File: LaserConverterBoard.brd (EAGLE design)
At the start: 100 x 80 mm, 49 parts, among them J10 24V, J11 FAN, J12 E-STOP, J3 04-JST-B4B-XH-A, J4 04-JST-B4B-XH-A, J5 04-JST-B4B-XH-A, J6 X, J7 Y, J8 Z-STOP, Q1 FDN5630, Q2 FDN5630, U10 REE-0505S, Y1 POLOLU_A4988, Y2 POLOLU_A4988, Y3 POLOLU_A4988

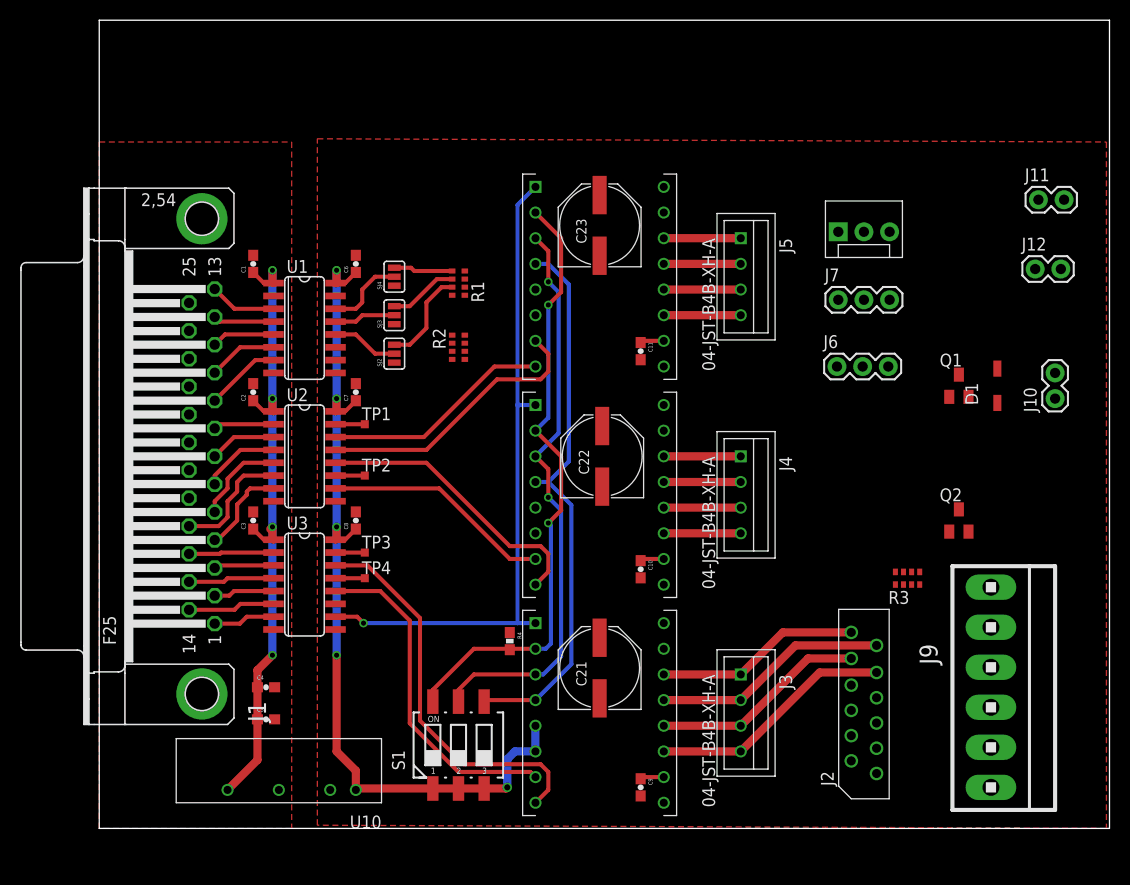
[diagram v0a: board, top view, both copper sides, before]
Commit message: Hand routing of board 1.3 complete. Still needs silk screening done.
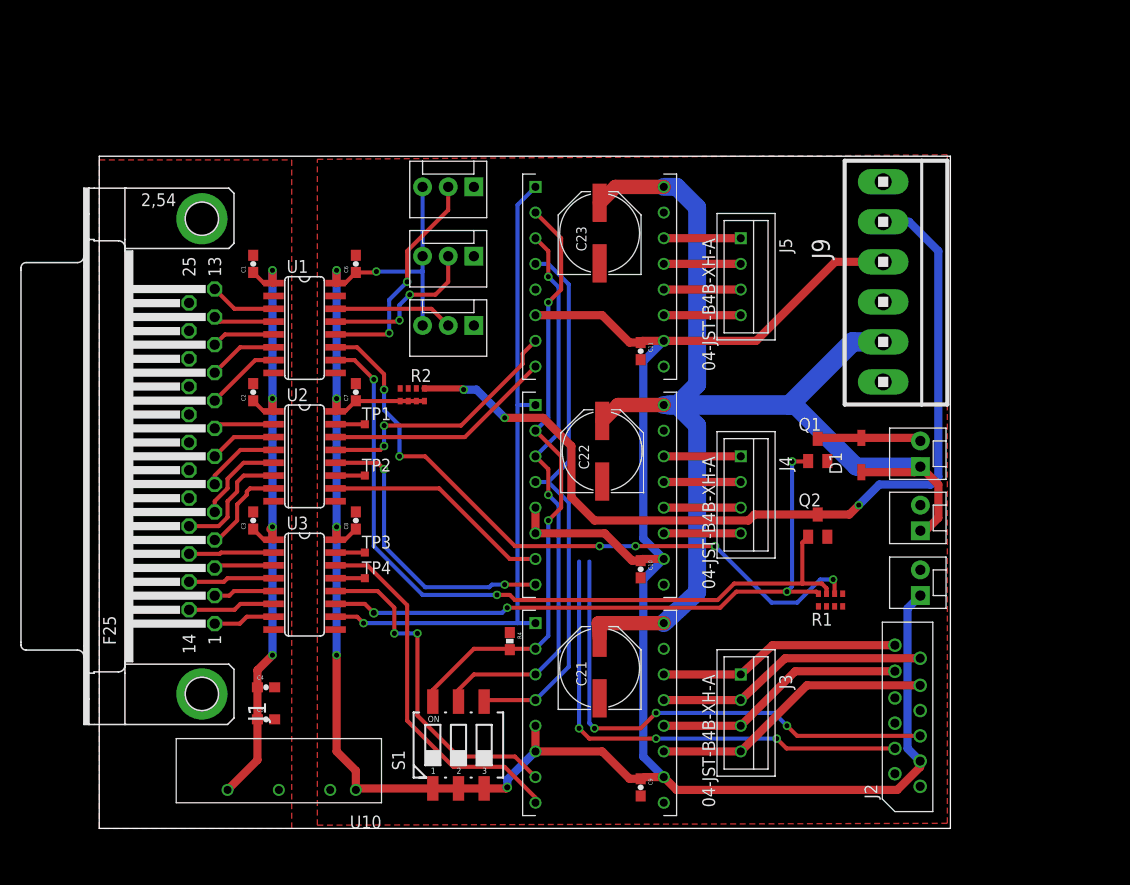
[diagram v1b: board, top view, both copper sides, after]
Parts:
- removed R3: 4.7K, SparkFun-Resistors:0603-ARV
- removed SJ2, SJ3, SJ4: (no value), SparkFun-Passives:SJ_3
- J10: value 24V -> AIR; device SparkFun-Connectors:1X02 -> SparkFun-Connectors:MOLEX-1X2
- J11, J12: device SparkFun-Connectors:1X02 -> SparkFun-Connectors:MOLEX-1X2
- J6, J7: device SparkFun-Connectors:1X03 -> SparkFun-Connectors:MOLEX-1X3
- moved R1 48.4 mm to (72.4, 22.6), turned to 0 degrees
- moved J9 41.5 mm to (77.6, 54.1)
- moved J8 36.3 mm to (37.1, 63.5), turned to 180 degrees
- moved J7 36.3 mm to (37.1, 56.6), turned to 180 degrees
- moved J6 36.2 mm to (37.1, 49.8), turned to 180 degrees
- moved J11 34.8 mm to (81.3, 29.5), turned to 90 degrees
- moved J12 34.3 mm to (81.3, 23.1), turned to 90 degrees
- moved Q1 15.3 mm to (71.1, 37.5)
- moved D1 15.1 mm to (75.4, 37.0)
- moved J10 14.9 mm to (81.3, 35.8)
- moved Q2 14.0 mm to (71.1, 30.0)
- moved R2 6.56 mm to (31.0, 42.9), turned to 180 degrees
- moved J2 4.50 mm to (80.0, 10.4)
- moved C23 0.76 mm to (49.5, 58.9)
- moved C22 0.51 mm to (49.8, 37.3)
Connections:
- removed net N$1: R1.7, SJ2.3
- removed net N$2: R1.6, SJ3.3
- removed net N$3: R2.4, SJ2.1
- removed net N$4: R2.3, SJ3.1
- removed net N$5: R2.2, SJ4.1
- removed net N$6: R1.5, SJ4.3
- net AIR_EN_ISO: now also R1.8; no longer R3.8
- net CNC_GND: no longer R1.4, R3.1, R3.2
- net ESTOP_ISO: now also R1.6; no longer R1.8
- net LASER_ISO: now also R1.7; no longer R3.7
- net XLIM_ISO: now also R2.2; no longer SJ4.2
- net YLIM_ISO: now also R2.3; no longer SJ3.2
- net ZLIM_ISO: now also R2.4; no longer SJ2.2
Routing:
- net CNC_5V: track 94.1 -> 273.6 mm, vias 5 -> 6
- net CNC_24V: track 0.00 -> 124.8 mm
- net LASER: track 0.00 -> 90.1 mm, vias 0 -> 3
- net LASER_ISO: track 0.00 -> 74.4 mm, vias 0 -> 2
- net ESTOP_ISO: track 0.00 -> 66.0 mm, vias 0 -> 6
- net AIR_EN_ISO: track 0.00 -> 63.8 mm, vias 0 -> 4
- net YLIM_ISO: track 6.08 -> 64.8 mm, vias 0 -> 5
- net XLIM_ISO: track 7.88 -> 62.4 mm, vias 0 -> 3
- net ZLIM_ISO: track 6.61 -> 22.3 mm, vias 0 -> 2
- net N$8: track 0.00 -> 10.3 mm
- net N$1: track 9.57 -> 0.00 mm
- net N$2: track 6.84 -> 0.00 mm
- net N$6: track 5.86 -> 0.00 mm
- net X_B-: track 24.3 -> 28.1 mm
- net X_B+: track 21.3 -> 25.1 mm
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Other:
- board size 100 x 80 mm -> 84.3 x 66.5 mm

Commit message: Silk screen done, could use a Chimera Logo on it, IMO
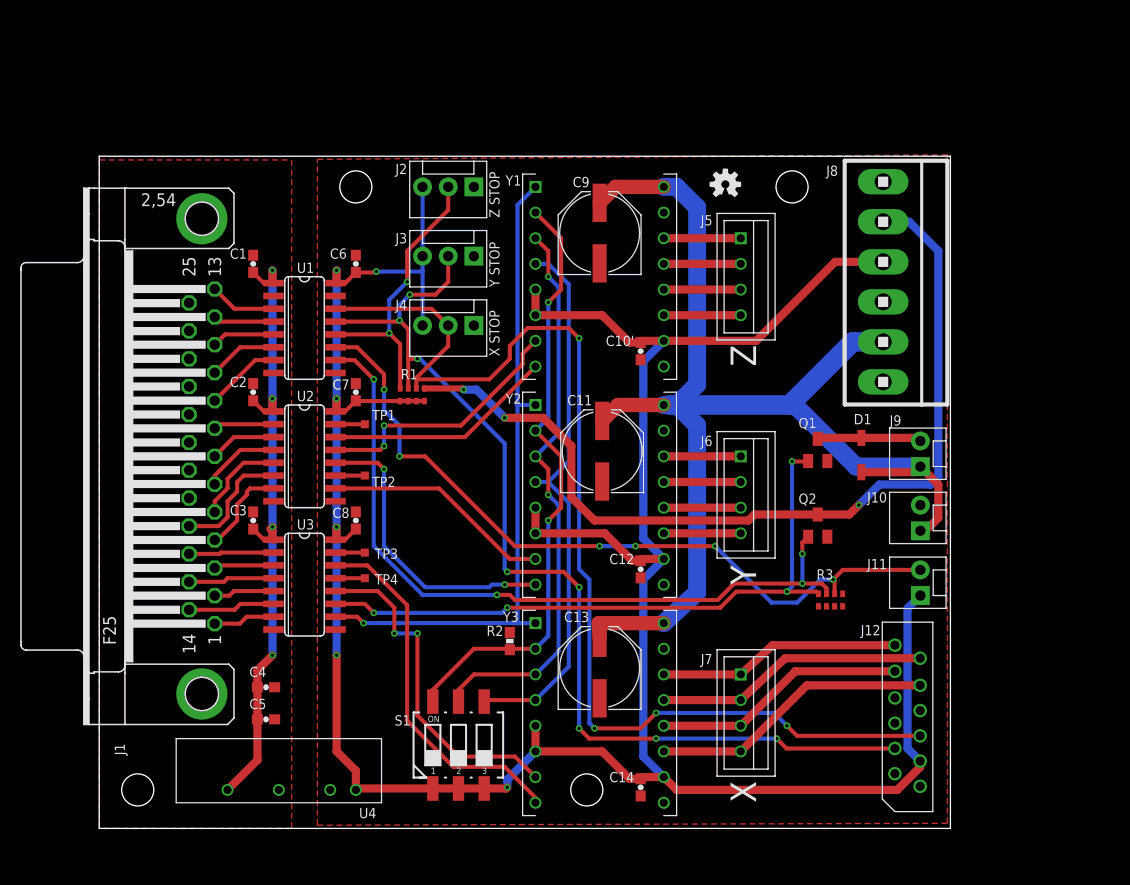
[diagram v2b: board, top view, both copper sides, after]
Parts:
- removed C22, C23: 47uF, rcl:PANASONIC_E
- removed R4: 100k, SparkFun-Resistors:0603-RES
- added C10', C14: 1nF, SparkFun-Capacitors:0603-CAP
- added LOGO1: OSHW-LOGOS, SparkFun-Aesthetics:OSHW-LOGO-S
- added R3: 4.7K, SparkFun-Resistors:0603-ARV
- C11, C9: value 1nF -> 47uF; device SparkFun-Capacitors:0603-CAP -> rcl:PANASONIC_E
- J10: value AIR -> FAN
- J11: value FAN -> E-STOP
- J12: value E-STOP -> (none); device SparkFun-Connectors:MOLEX-1X2 -> con-amp-te:12P
- J2: value (none) -> Z-STOP; device con-amp-te:12P -> SparkFun-Connectors:MOLEX-1X3
- J3: value 04-JST-B4B-XH-A -> Y; device con-jst-xh:B4B-XH -> SparkFun-Connectors:MOLEX-1X3
- J4: value 04-JST-B4B-XH-A -> X; device con-jst-xh:B4B-XH -> SparkFun-Connectors:MOLEX-1X3
- J6: value X -> 04-JST-B4B-XH-A; device SparkFun-Connectors:MOLEX-1X3 -> con-jst-xh:B4B-XH
- J7: value Y -> 04-JST-B4B-XH-A; device SparkFun-Connectors:MOLEX-1X3 -> con-jst-xh:B4B-XH
- J8: value Z-STOP -> (none); device SparkFun-Connectors:MOLEX-1X3 -> con-amp:1X6MTA
- J9: value (none) -> AIR; device con-amp:1X6MTA -> SparkFun-Connectors:MOLEX-1X2
- R2: value 4.7K -> 100k; device SparkFun-Resistors:0603-ARV -> SparkFun-Resistors:0603-RES
- moved J2 68.3 mm to (37.1, 63.5), turned to 180 degrees
- moved C9 55.0 mm to (49.5, 58.9), turned to 90 degrees
- moved J3 52.4 mm to (37.1, 56.6), turned to 180 degrees
- moved J7 52.4 mm to (63.5, 11.4), turned to 270 degrees
- moved R1 46.1 mm to (31.0, 42.9), turned to 180 degrees
- moved Y1 43.2 mm to (49.5, 54.6)
- moved Y3 43.2 mm to (49.5, 11.4)
- moved J8 41.6 mm to (77.6, 54.1), turned to 270 degrees
- moved J4 31.3 mm to (37.1, 49.8), turned to 180 degrees
- moved J6 31.3 mm to (63.5, 33.0), turned to 270 degrees
- moved R2 26.2 mm to (40.6, 18.5), turned to 270 degrees
- moved J9 18.7 mm to (81.3, 35.8), turned to 90 degrees
- moved J12 12.7 mm to (80.0, 10.4)
- moved C11 10.6 mm to (49.8, 37.3), turned to 90 degrees
- moved J11 6.41 mm to (81.3, 23.1)
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- renumbered C10 to C12, C21 to C13, U10 to U4
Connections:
- net AIR_EN_ISO: now also R3.8; no longer R1.8
- net CNC_24V: now also C11.+, C9.+, J8.2, J9.1; no longer C22.+, C23.+, J11.1, J9.2
- net CNC_5V: now also C10'.1, C14.1, J11.1, J12.3, J3.3, J4.3, J8.4, R1.5, R1.6, R1.7, R1.8; no longer C11.1, C9.1, J12.1, J6.3, J7.3, J8.3, J9.4, R2.5, R2.6, R2.7, R2.8
- net CNC_GND: now also C10'.2, C11.-, C14.2, C9.-, J10.2, J12.6, J2.1, J3.1, J4.1, J8.6, R2.1, R3.1, R3.2, R3.3; no longer C11.2, C22.-, C23.-, C9.2, J11.2, J2.6, J6.1, J7.1, J9.1, J9.6, R1.1, R1.2, R1.3, R4.1
- net ESTOP_ISO: now also J11.2, R3.6; no longer J12.2, R1.6
- net LASER: now also J8.5, R1.1; no longer J9.5, R2.1
- net LASER_ISO: now also R3.7; no longer R1.7
- net MS1: now also R2.2; no longer R4.2
- net N$8: now also J9.2; no longer J10.2
- net XDIR_ISO: now also Y3.DIR; no longer Y1.DIR
- net XLIM_ISO: now also J12.5, J4.2, R1.2; no longer J2.5, J6.2, R2.2
- net XSTP_ISO: now also Y3.STEP; no longer Y1.STEP
- net X_A+: now also J12.12, J7.P$1, Y3.2B; no longer J2.12, J3.P$1, Y1.2B
- net X_A-: now also J12.11, J7.P$2, Y3.2A; no longer J2.11, J3.P$2, Y1.2A
- net X_B+: now also J12.10, J7.P$3, Y3.1A; no longer J2.10, J3.P$3, Y1.1A
- net X_B-: now also J12.9, J7.P$4, Y3.1B; no longer J2.9, J3.P$4, Y1.1B
- net YLIM_ISO: now also J12.4, J3.2, R1.3; no longer J2.4, J7.2, R2.3
- net Y_A+: now also J6.P$1; no longer J4.P$1
- net Y_A-: now also J6.P$2; no longer J4.P$2
- net Y_B+: now also J6.P$3; no longer J4.P$3
- net Y_B-: now also J6.P$4; no longer J4.P$4
- net ZDIR_ISO: now also Y1.DIR; no longer Y3.DIR
- net ZLIM_ISO: now also J2.2, R1.4; no longer J8.2, R2.4
- net ZSTP_ISO: now also Y1.STEP; no longer Y3.STEP
- net Z_A+: now also Y1.2B; no longer Y3.2B
- net Z_A-: now also Y1.2A; no longer Y3.2A
- net Z_B+: now also Y1.1A; no longer Y3.1A
- net Z_B-: now also Y1.1B; no longer Y3.1B
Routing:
- net XLIM_ISO: track 62.4 -> 111.8 mm, vias 3 -> 4
- net YLIM_ISO: track 64.8 -> 102.9 mm, vias 5 -> 8
- net ESTOP_ISO: track 66.0 -> 75.0 mm
- net ZLIM_ISO: track 22.3 -> 28.2 mm
- net CNC_5V: track 273.6 -> 276.1 mm
- net LASER_ISO: vias 2 -> 4
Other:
- board text added: "J10"
- board text added: "J11"
- board text added: "J2"
- board text added: "J3"
- board text added: "J4"
- board text added: "J9"
- board text added: "X"
- board text added: "X STOP"
- board text added: "Y"
- board text added: "Y STOP"
- board text added: "Z"
- board text added: "Z STOP"
